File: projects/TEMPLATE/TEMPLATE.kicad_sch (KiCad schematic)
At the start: 0 parts

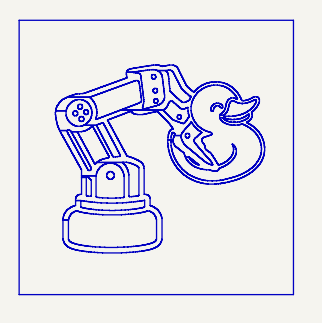
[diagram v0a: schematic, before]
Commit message: Rename template -> TEMPLATE, fix graphics
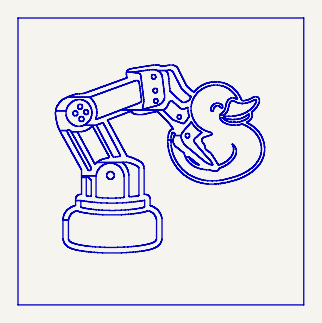
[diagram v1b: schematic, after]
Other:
- title: Project title -> project title
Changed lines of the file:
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@@
 	(paper "A4")
 	(title_block
-		(title "Project title")
+		(title "project title")
 		(date "2025-09-29")
 		(rev "0.1")
 		(company "Manuel Heredia - sevillabot")
-		(comment 1 "Description Line 2")
-		(comment 2 "Description Line 1")
+		(comment 1 "description line 2")
+		(comment 2 "descrition line 1")
 		(comment 3 "KiCAD like a Pro - Udemy Course (Project XX)")
 	)
@@
 	)
 	(rectangle
-		(start 145.415 166.37)
-		(end 175.895 196.85)
+		(start 145.288 166.116)
+		(end 177.038 197.993)
 		(stroke
 			(width 0)
